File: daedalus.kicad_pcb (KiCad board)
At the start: 4 copper layers, 42 x 50.2 mm, 100 parts, among them J1 CAN Bus, J2 CAN Bus, J5 A Terminal, J6 B Terminal, J7 C Terminal, J9 USB_B_Micro, Q1 AO3401A, U1 XT30, U10 TPH, U11 TPH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

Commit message: Finished preliminary BOM
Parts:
- C10, C6, C7, C8, C9: value 100 nF -> 100nF
- C11, C23, C24: footprint Capacitor_SMD:C_0603_1608Metric -> Capacitor_SMD:C_0402_1005Metric
- C12: value 1uF -> 1uF, 10V
- C13: value 10nF -> 10nF, 10V
- C19, C20: value 2.2 uF -> 2.2uF, 10V
- C25, C26: value 12 pF -> 12pF, 10V

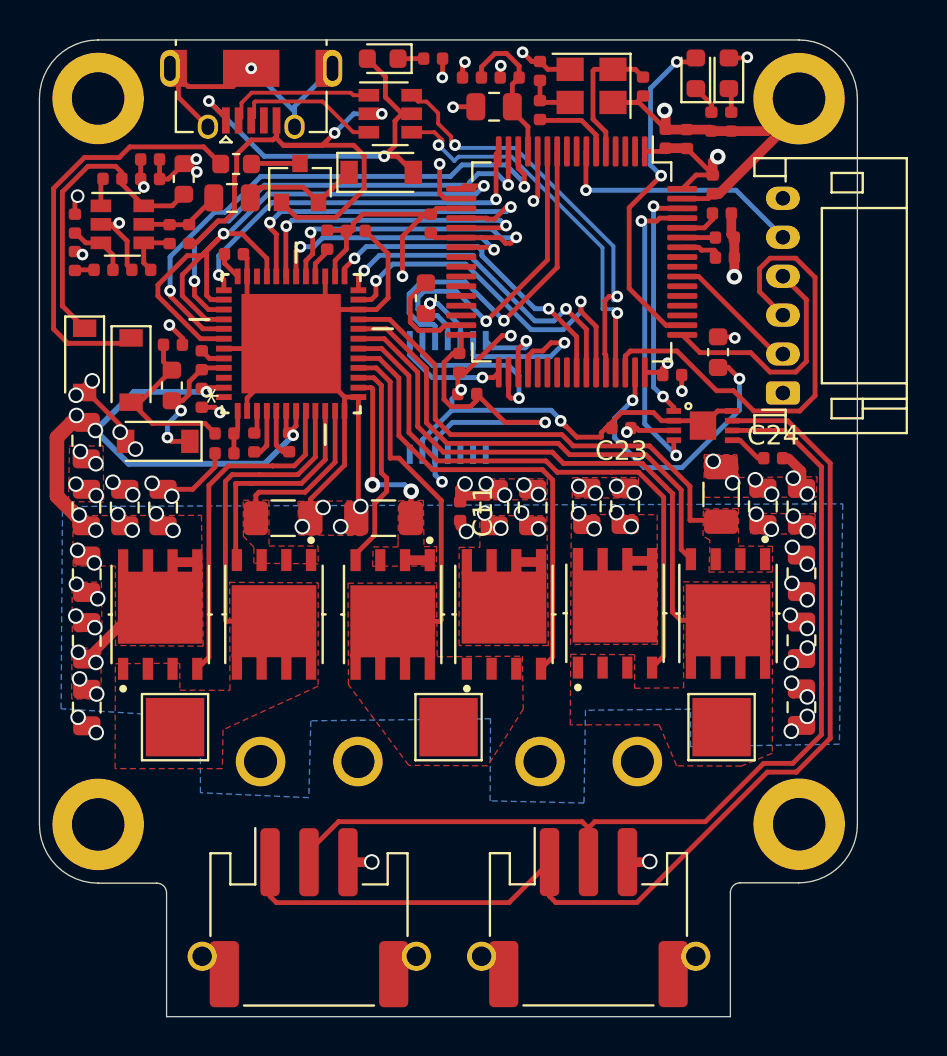
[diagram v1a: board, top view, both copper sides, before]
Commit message: Updated vias, added vias, removed i2c line and pullups, added renders
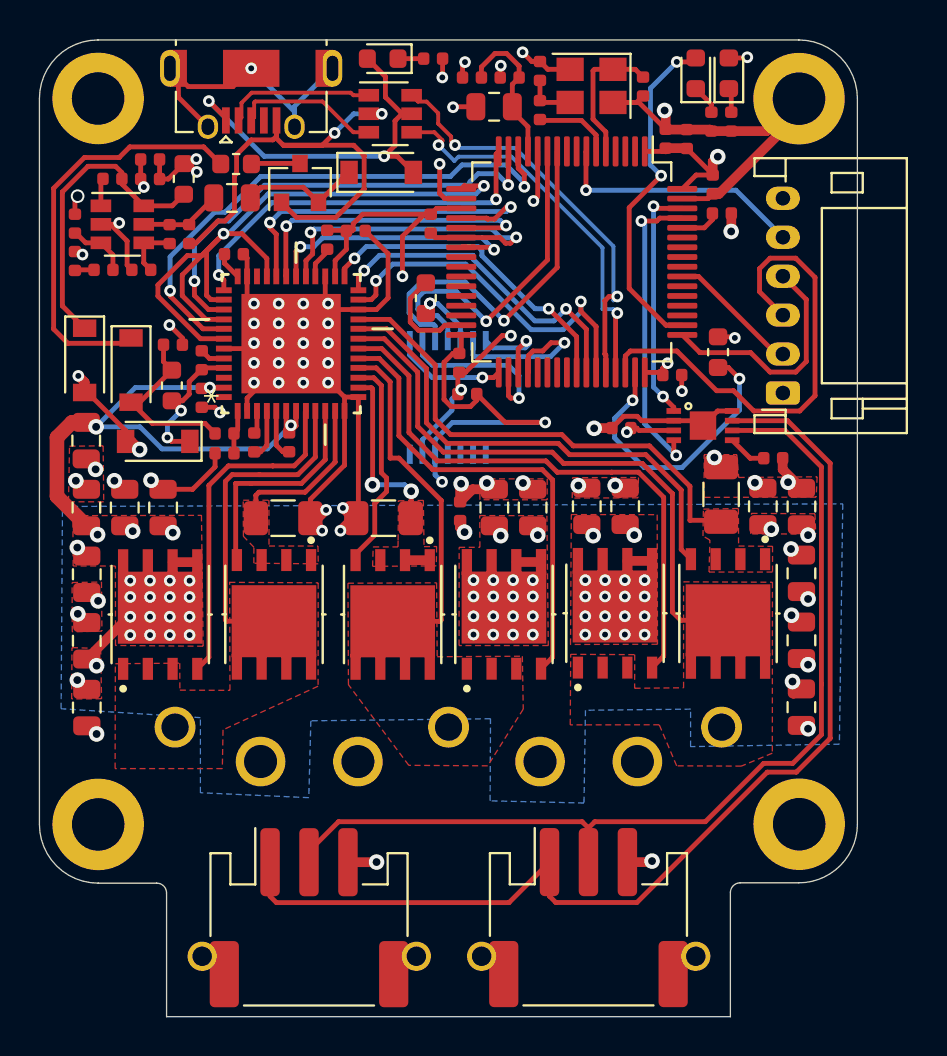
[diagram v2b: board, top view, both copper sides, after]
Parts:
- removed R8, R9: 2k2, Resistor_SMD:R_0402_1005Metric
- added G***: LOGO, daedalus_kicad_lib:daedalus, B.Cu at (144.0, 85.5)
- C10, C6, C7, C8, C9: value 100nF -> 0.1uF, 10V
- C2, C3, C4: value 10uF -> 10uF, 10V
- J5, J6, J7: footprint TestPoint:TestPoint_Pad_3.0x3.0mm -> daedalus_kicad_lib:18_AWG_PAD
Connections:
- U7 pad 58: I2C1_SCL -> Net-(U7-Pad58)
- U7 pad 59: I2C1_SDA -> Net-(U7-Pad59)
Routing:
- net BGND: track 184.9 -> 169.1 mm, vias 66 -> 67
- net VIN: track 58.0 -> 49.0 mm, vias 34 -> 66
- net VDD: track 55.1 -> 53.0 mm
- net I2C1_SCL: track 1.93 -> 0.00 mm
- net I2C1_SDA: track 1.70 -> 0.00 mm
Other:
- board text added: "Jeremy Kanovsky & Eric Wu Daedalus v1.0"
